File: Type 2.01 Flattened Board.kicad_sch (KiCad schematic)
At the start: 6 parts

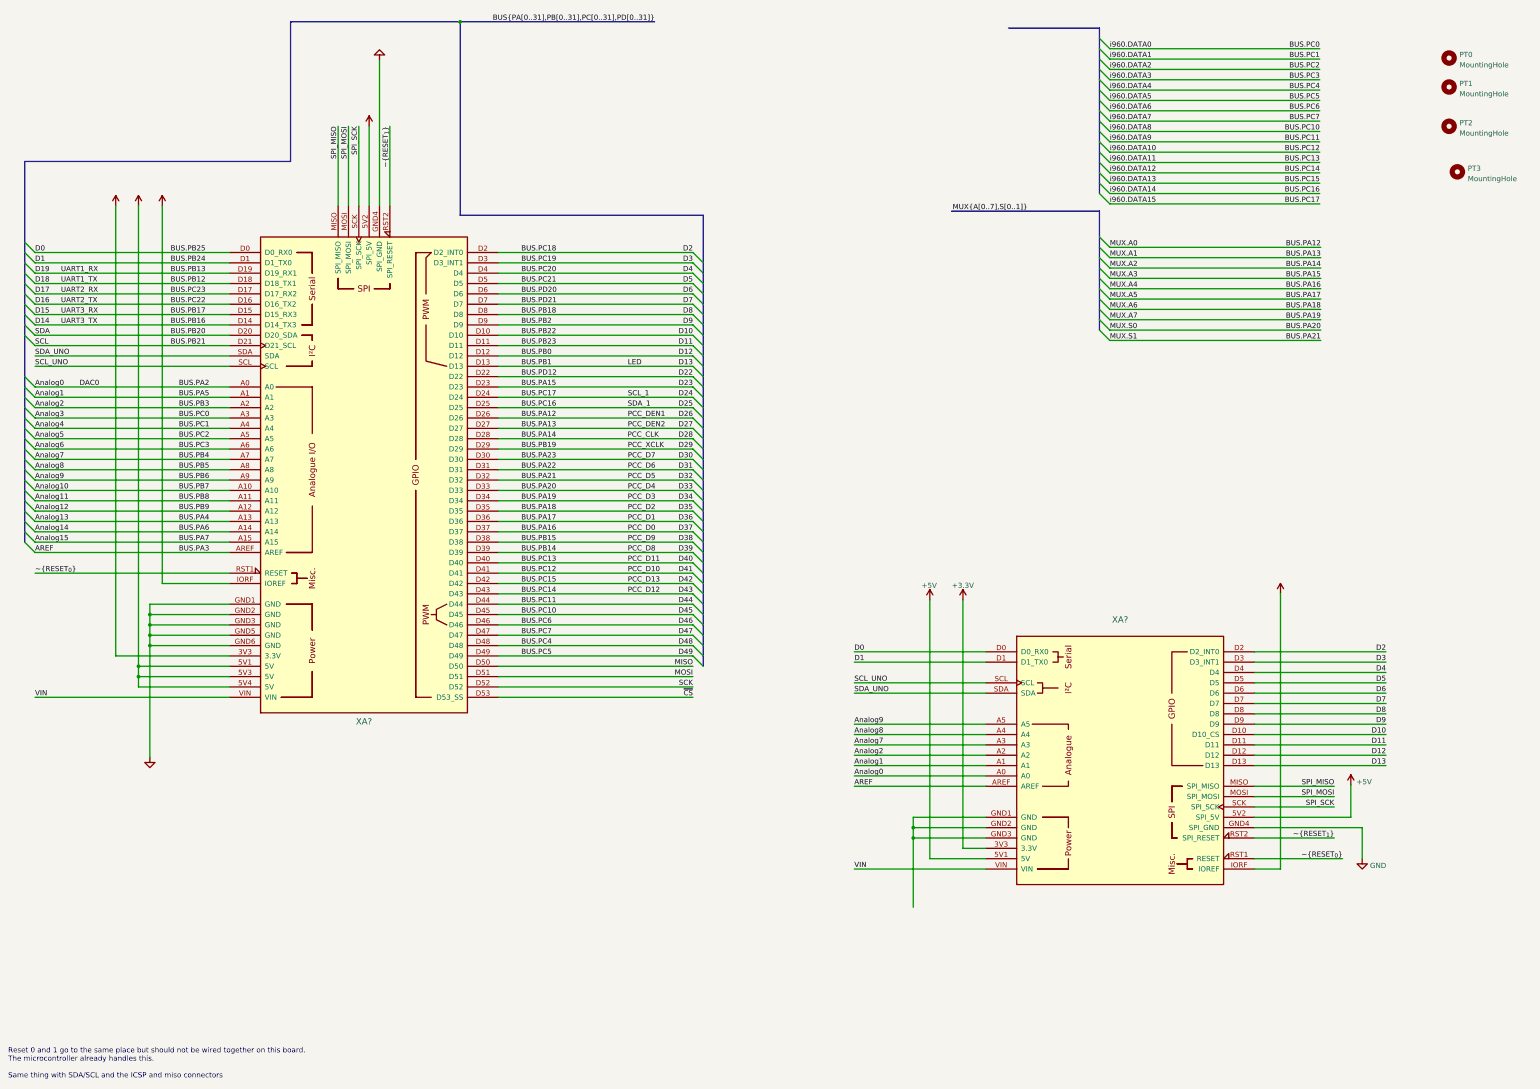
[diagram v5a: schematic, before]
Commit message: Added CCL connections as text
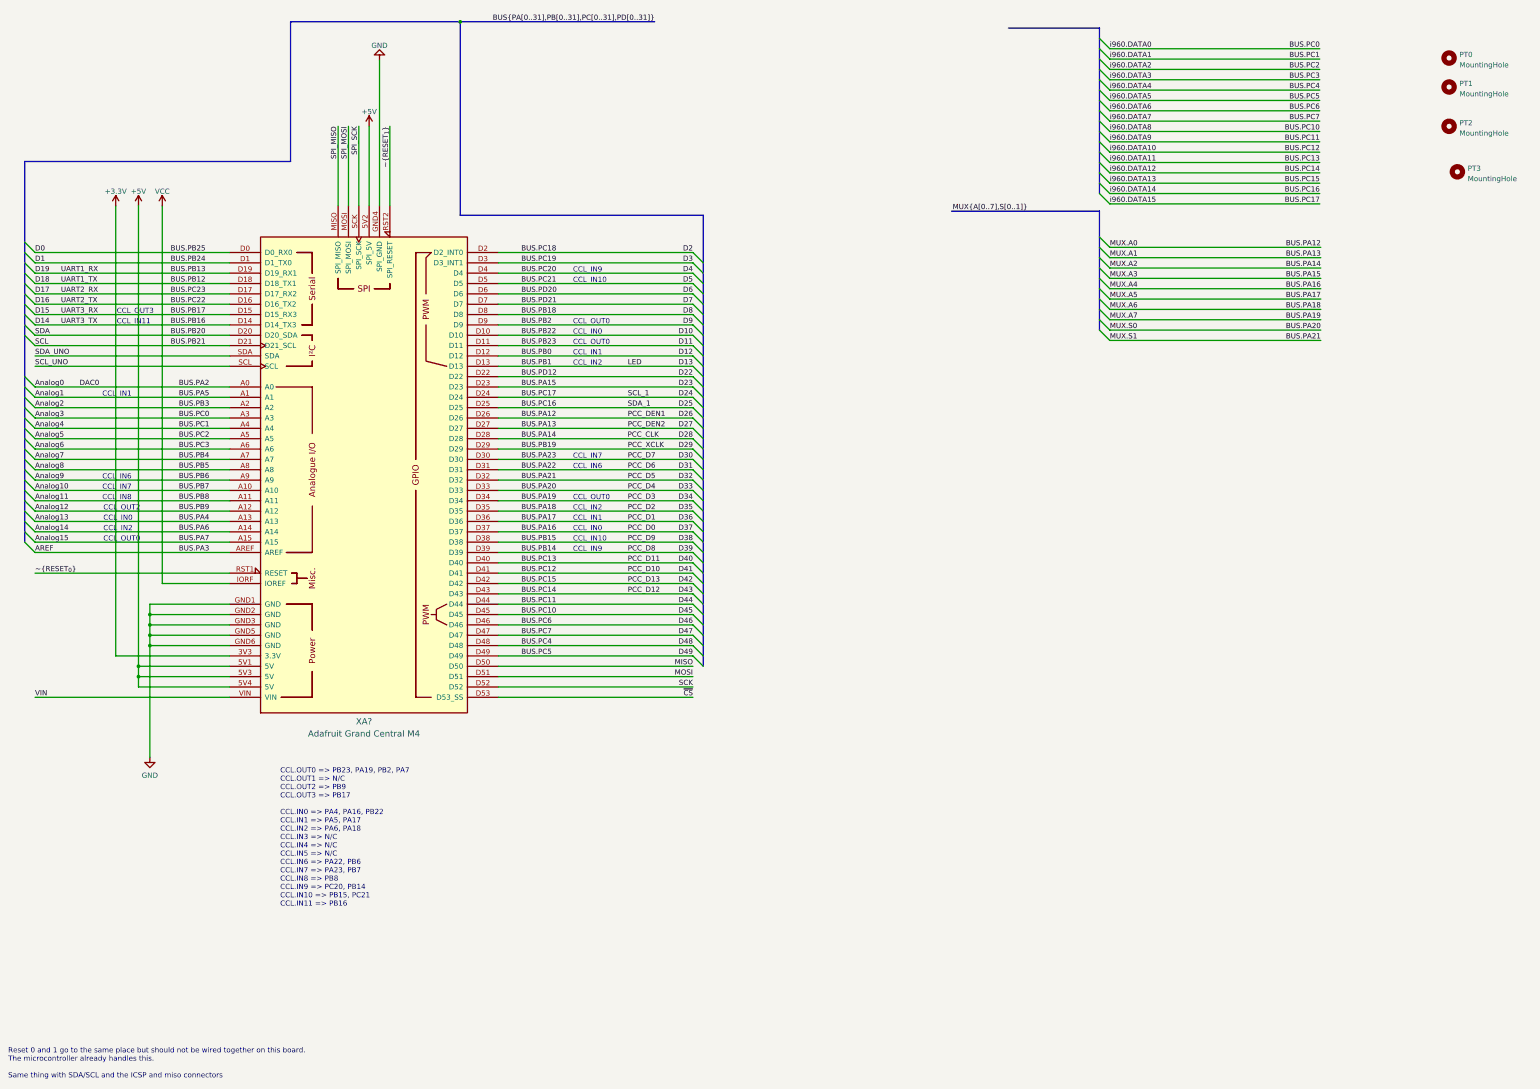
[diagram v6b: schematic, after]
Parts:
- removed XA?: (no value), symbol arduino_alarm_siren:Arduino_Uno_Shield
- XA?: value (none) -> Adafruit Grand Central M4; footprint (none) -> Arduino_Alarm_Siren:Arduino_Mega2560_Shield
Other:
- note added: "CCL.OUT0 => PB23, PA19, PB2, PA7 CCL.OUT1 => N/C CCL.OUT2 => PB9 CCL.OUT3 => PB17 CCL.IN0 => PA4, PA16, PB22 CCL.IN1 => PA5, PA17 CCL.IN2 => PA6, PA18 CCL.IN3 => N/C CCL.IN4 => N/C CCL.IN5 => N/C CCL.IN6 => PA22, PB6 CCL.IN7 => PA23, PB7 CCL.IN8 => PB8 CCL.IN9 => PC20, PB14 CCL.IN10 => PB15, PC21 CCL.IN11 => PB16"
- note added: "CCL_IN0"
- note added: "CCL_IN1"
- note added: "CCL_IN10"
- note added: "CCL_IN11"
- note added: "CCL_IN2"
- note added: "CCL_IN6"
- note added: "CCL_IN7"
- note added: "CCL_IN8"
- note added: "CCL_IN9"
- note added: "CCL_OUT0"
- note added: "CCL_OUT2"
- note added: "CCL_OUT3"

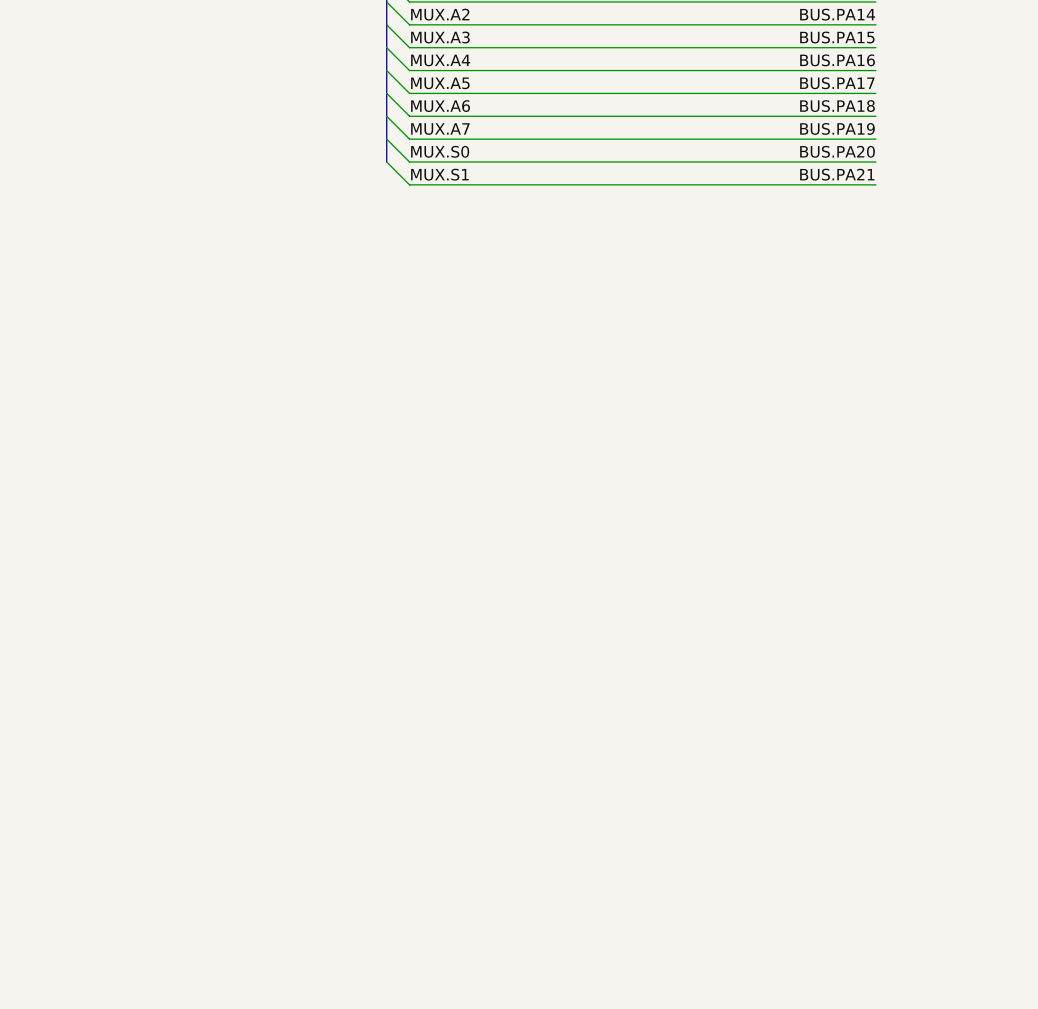
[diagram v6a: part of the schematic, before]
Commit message: Start defining the mux input and drop the uno connector for now
I need a working board first
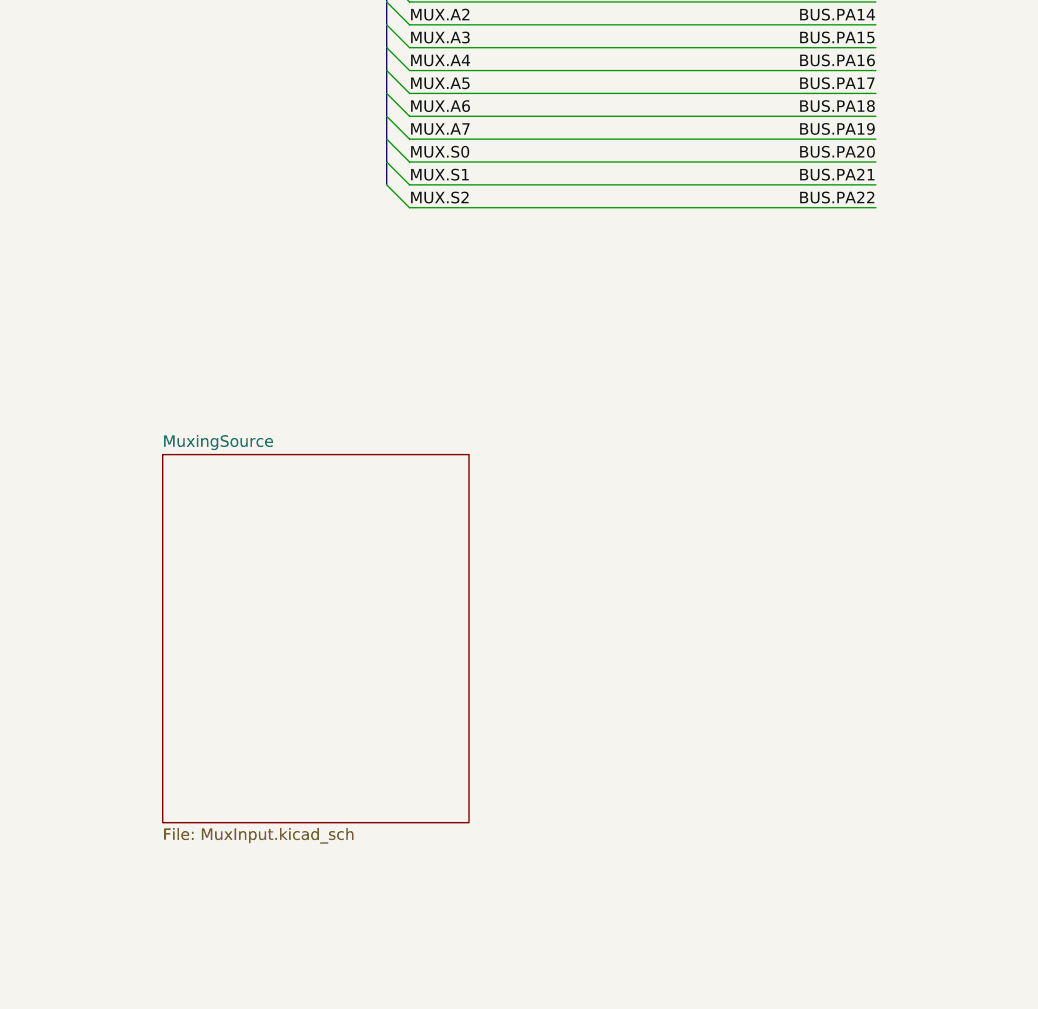
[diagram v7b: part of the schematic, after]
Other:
- added sheet MuxingSource (MuxInput.kicad_sch)
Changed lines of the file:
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@@
+    (stroke (width 0) (type default) (color 0 0 0 0))
+  )
+  (bus_entry (at 287.274 94.742) (size 2.54 2.54)
     (stroke (width 0) (type default) (color 0 0 0 0))
   )
@@
     (stroke (width 0) (type default) (color 0 0 0 0))
   )
+  (bus (pts (xy 287.274 38.354) (xy 287.274 35.814))
+    (stroke (width 0) (type default) (color 0 0 0 0))
+  )
+  (bus (pts (xy 287.274 56.134) (xy 287.274 53.594))
+    (stroke (width 0) (type default) (color 0 0 0 0))
+  )
+  (bus (pts (xy 23.368 73.152) (xy 23.368 70.612))
+    (stroke (width 0) (type default) (color 0 0 0 0))
+  )
+  (wire (pts (xy 139.7 179.832) (xy 187.452 179.832))
+    (stroke (width 0) (type default) (color 0 0 0 0))
+  )
+  (wire (pts (xy 289.814 48.514) (xy 341.376 48.514))
+    (stroke (width 0) (type default) (color 0 0 0 0))
+  )
+  (wire (pts (xy 139.7 98.552) (xy 187.452 98.552))
+    (stroke (width 0) (type default) (color 0 0 0 0))
+  )
+  (wire (pts (xy 51.308 174.752) (xy 73.66 174.752))
+    (stroke (width 0) (type default) (color 0 0 0 0))
+  )
+  (wire (pts (xy 25.908 113.792) (xy 73.66 113.792))
+    (stroke (width 0) (type default) (color 0 0 0 0))
+  )
+  (bus (pts (xy 287.274 87.122) (xy 287.274 84.582))
+    (stroke (width 0) (type default) (color 0 0 0 0))
+  )
+  (bus (pts (xy 88.646 50.8) (xy 88.646 16.51))
+    (stroke (width 0) (type default) (color 0 0 0 0))
+  )
+  (bus (pts (xy 287.274 92.202) (xy 287.274 94.742))
+    (stroke (width 0) (type default) (color 0 0 0 0))
+  )
+  (wire (pts (xy 289.814 33.274) (xy 341.376 33.274))
+    (stroke (width 0) (type default) (color 0 0 0 0))
+  )
+  (wire (pts (xy 25.908 93.472) (xy 73.66 93.472))
+    (stroke (width 0) (type default) (color 0 0 0 0))
+  )
+  (bus (pts (xy 23.368 121.412) (xy 23.368 118.872))
+    (stroke (width 0) (type default) (color 0 0 0 0))
+  )
+  (wire (pts (xy 25.908 101.092) (xy 73.66 101.092))
+    (stroke (width 0) (type default) (color 0 0 0 0))
+  )
+  (bus (pts (xy 23.368 123.952) (xy 23.368 121.412))
+    (stroke (width 0) (type default) (color 0 0 0 0))
+  )
+  (bus (pts (xy 23.368 136.652) (xy 23.368 134.112))
+    (stroke (width 0) (type default) (color 0 0 0 0))
+  )
+  (wire (pts (xy 54.102 162.052) (xy 54.102 164.592))
+    (stroke (width 0) (type default) (color 0 0 0 0))
+  )
+  (bus (pts (xy 189.992 159.512) (xy 189.992 162.052))
+    (stroke (width 0) (type default) (color 0 0 0 0))
+  )
+  (wire (pts (xy 289.814 40.894) (xy 341.376 40.894))
+    (stroke (width 0) (type default) (color 0 0 0 0))
+  )
+  (bus (pts (xy 23.368 80.772) (xy 23.368 78.232))
+    (stroke (width 0) (type default) (color 0 0 0 0))
+  )
+  (bus (pts (xy 287.274 51.054) (xy 287.274 48.514))
+    (stroke (width 0) (type default) (color 0 0 0 0))
+  )
+  (wire (pts (xy 139.7 103.632) (xy 187.452 103.632))
+    (stroke (width 0) (type default) (color 0 0 0 0))
+  )
   (wire (pts (xy 289.814 94.742) (xy 341.63 94.742))
     (stroke (width 0) (type default) (color 0 0 0 0))
   )
-  (bus (pts (xy 287.274 38.354) (xy 287.274 35.814))
-    (stroke (width 0) (type default) (color 0 0 0 0))
-  )
-  (bus (pts (xy 287.274 56.134) (xy 287.274 53.594))
-    (stroke (width 0) (type default) (color 0 0 0 0))
-  )
-  (bus (pts (xy 23.368 73.152) (xy 23.368 70.612))
-    (stroke (width 0) (type default) (color 0 0 0 0))
-  )
-  (wire (pts (xy 139.7 179.832) (xy 187.452 179.832))
-    (stroke (width 0) (type default) (color 0 0 0 0))
-  )
-  (wire (pts (xy 289.814 48.514) (xy 341.376 48.514))
-    (stroke (width 0) (type default) (color 0 0 0 0))
-  )
-  (wire (pts (xy 139.7 98.552) (xy 187.452 98.552))
-    (stroke (width 0) (type default) (color 0 0 0 0))
-  )
-  (wire (pts (xy 51.308 174.752) (xy 73.66 174.752))
-    (stroke (width 0) (type default) (color 0 0 0 0))
-  )
-  (wire (pts (xy 25.908 113.792) (xy 73.66 113.792))
-    (stroke (width 0) (type default) (color 0 0 0 0))
-  )
-  (bus (pts (xy 287.274 87.122) (xy 287.274 84.582))
-    (stroke (width 0) (type default) (color 0 0 0 0))
-  )
-  (bus (pts (xy 88.646 50.8) (xy 88.646 16.51))
-    (stroke (width 0) (type default) (color 0 0 0 0))
-  )
-  (wire (pts (xy 289.814 33.274) (xy 341.376 33.274))
-    (stroke (width 0) (type default) (color 0 0 0 0))
-  )
-  (wire (pts (xy 25.908 93.472) (xy 73.66 93.472))
-    (stroke (width 0) (type default) (color 0 0 0 0))
-  )
-  (bus (pts (xy 23.368 121.412) (xy 23.368 118.872))
-    (stroke (width 0) (type default) (color 0 0 0 0))
-  )
-  (wire (pts (xy 25.908 101.092) (xy 73.66 101.092))
-    (stroke (width 0) (type default) (color 0 0 0 0))
-  )
-  (bus (pts (xy 23.368 123.952) (xy 23.368 121.412))
-    (stroke (width 0) (type default) (color 0 0 0 0))
-  )
-  (bus (pts (xy 23.368 136.652) (xy 23.368 134.112))
-    (stroke (width 0) (type default) (color 0 0 0 0))
-  )
-  (wire (pts (xy 54.102 162.052) (xy 54.102 164.592))
-    (stroke (width 0) (type default) (color 0 0 0 0))
-  )
-  (bus (pts (xy 189.992 159.512) (xy 189.992 162.052))
-    (stroke (width 0) (type default) (color 0 0 0 0))
-  )
-  (wire (pts (xy 289.814 40.894) (xy 341.376 40.894))
-    (stroke (width 0) (type default) (color 0 0 0 0))
-  )
-  (bus (pts (xy 23.368 80.772) (xy 23.368 78.232))
-    (stroke (width 0) (type default) (color 0 0 0 0))
-  )
-  (bus (pts (xy 287.274 51.054) (xy 287.274 48.514))
-    (stroke (width 0) (type default) (color 0 0 0 0))
-  )
-  (wire (pts (xy 139.7 103.632) (xy 187.452 103.632))
-    (stroke (width 0) (type default) (color 0 0 0 0))
-  )
   (wire (pts (xy 289.814 56.134) (xy 341.376 56.134))
     (stroke (width 0) (type default) (color 0 0 0 0))
@@
   )
   (bus (pts (xy 189.992 151.892) (xy 189.992 154.432))
+    (stroke (width 0) (type default) (color 0 0 0 0))
+  )
+  (wire (pts (xy 289.814 97.282) (xy 341.63 97.282))
     (stroke (width 0) (type default) (color 0 0 0 0))
   )
@@
     (effects (font (size 1.27 1.27)) (justify left bottom))
   )
+  (label "MUX.S2" (at 289.814 97.282 0)
+    (effects (font (size 1.27 1.27)) (justify left bottom))
+  )
   (label "MUX.A3" (at 289.814 79.502 0)
     (effects (font (size 1.27 1.27)) (justify left bottom))
@@
   (label "BUS.PC5" (at 145.288 172.212 0)
     (effects (font (size 1.27 1.27)) (justify left bottom))
+  )
+  (label "BUS.PA22" (at 341.63 97.282 180)
+    (effects (font (size 1.27 1.27)) (justify right bottom))
   )
   (label "BUS.PA13" (at 341.63 74.422 180)
@@
     (pin "1")
   )
+  (sheet (at 262.382 124.714) (size 34.036 40.894) (fields_autoplaced)
+    (stroke (width 0.1524) (type solid) (color 0 0 0 0))
+    (fill (color 0 0 0 0.0000))
+    (property "Sheet name" "MuxingSource" (id 0) (at 262.382 124.0024 0)
+      (effects (font (size 1.27 1.27)) (justify left bottom))
+    )
+    (property "Sheet file" "MuxInput.kicad_sch" (id 1) (at 262.382 166.1926 0)
+      (effects (font (size 1.27 1.27)) (justify left top))
+    )
+  )
   (sheet_instances
     (path "/" (page "1"))
+    (path "/79441cfe-3899-4d3b-8b0d-5ff45c5633da" (page "2"))
+    (path "/79441cfe-3899-4d3b-8b0d-5ff45c5633da/91a24060-cf18-40fd-b368-13c3d62154ef" (page "3"))
   )
   (symbol_instances
@@
       (reference "#PWR?") (unit 1) (value "GND") (footprint "")
     )
+    (path "/79441cfe-3899-4d3b-8b0d-5ff45c5633da/91a24060-cf18-40fd-b368-13c3d62154ef/4b7dd3ba-8c48-4927-bacd-b327e612fdd1"
+      (reference "#PWR?") (unit 1) (value "VCC") (footprint "")
+    )
+    (path "/79441cfe-3899-4d3b-8b0d-5ff45c5633da/91a24060-cf18-40fd-b368-13c3d62154ef/531ccfb8-083a-4e78-8462-f015f9d0487b"
+      (reference "#PWR?") (unit 1) (value "GND") (footprint "")
+    )
     (path "/6bbc0ffb-1253-4f83-a391-18c95b6a41d8"
       (reference "#PWR?") (unit 1) (value "+5V") (footprint "")
@@
       (reference "#PWR?") (unit 1) (value "+3.3V") (footprint "")
     )
+    (path "/79441cfe-3899-4d3b-8b0d-5ff45c5633da/91a24060-cf18-40fd-b368-13c3d62154ef/f32b8ff4-8fac-4e98-9053-183e1380bc78"
+      (reference "C?") (unit 1) (value "0.1uF") (footprint "")
+    )
     (path "/449a4130-5198-43c7-aa17-3cb30c17454b"
       (reference "PT0") (unit 1) (value "MountingHole") (footprint "MountingHole:MountingHole_3.2mm_M3_ISO14580_Pad")
@@
       (reference "PT3") (unit 1) (value "MountingHole") (footprint "MountingHole:MountingHole_3.2mm_M3_ISO14580_Pad")
     )
+    (path "/79441cfe-3899-4d3b-8b0d-5ff45c5633da/49e96dac-9f28-46ad-8b8c-f17561a3a0e1"
+      (reference "U?") (unit 1) (value "74LS158") (footprint "")
+    )
+    (path "/79441cfe-3899-4d3b-8b0d-5ff45c5633da/91a24060-cf18-40fd-b368-13c3d62154ef/651fa084-9ad9-4a74-a5ae-11bfbf98411b"
+      (reference "U?") (unit 1) (value "74AHC158") (footprint "")
+    )
+    (path "/79441cfe-3899-4d3b-8b0d-5ff45c5633da/afa97cc7-19e1-46c3-b3d2-42d6237c8de4"
+      (reference "U?") (unit 1) (value "74LS158") (footprint "")
+    )
     (path "/2bd6b25f-a519-4224-8dd9-2e42d262ce2e"
